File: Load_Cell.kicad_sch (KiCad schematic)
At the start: 1 part, among them J1 Conn_01x04

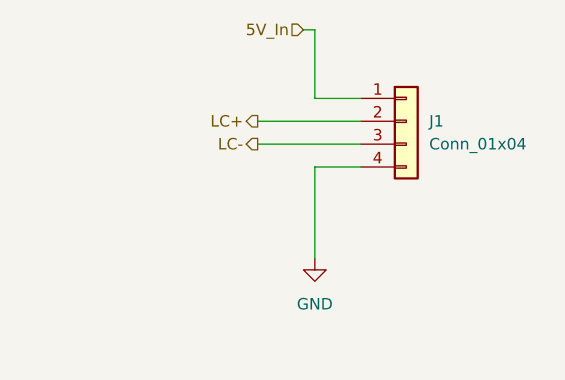
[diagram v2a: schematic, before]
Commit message: fix load cell connector
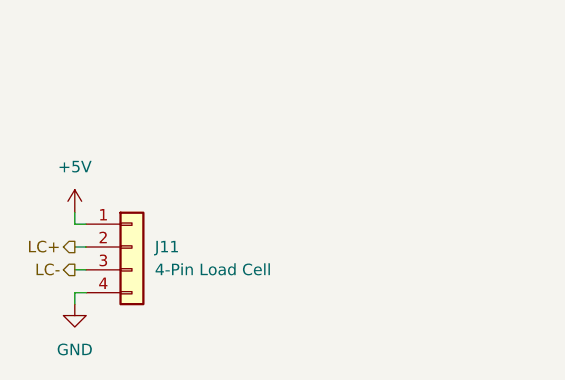
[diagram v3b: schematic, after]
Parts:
- removed J1: Conn_01x04, Connector_JST:JST_EH_B4B-EH-A_1x04_P2.50mm_Vertical, symbol Connector_Generic:Conn_01x04
- added J11: 4-Pin Load Cell, Connector_Molex:Molex_Micro-Fit_3.0_43650-0415_1x04_P3.00mm_Vertical, symbol Connector_Generic:Conn_01x04
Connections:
- net GND: now also J11.4 (Pin_4)
- net LC+: now also J11.2 (Pin_2)
- net LC-: now also J11.3 (Pin_3)
- new net +5V: J11.1 (Pin_1)
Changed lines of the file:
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@@
 	(wire
 		(pts
-			(xy 165.1 82.55) (xy 170.18 82.55)
-		)
-		(stroke
-			(width 0)
-			(type default)
-		)
-	)
-	(wire
-		(pts
-			(xy 163.83 74.93) (xy 165.1 74.93)
-		)
-		(stroke
-			(width 0)
-			(type default)
-		)
-	)
-	(wire
-		(pts
-			(xy 158.75 87.63) (xy 170.18 87.63)
-		)
-		(stroke
-			(width 0)
-			(type default)
-		)
-	)
-	(wire
-		(pts
-			(xy 165.1 100.33) (xy 165.1 90.17)
-		)
-		(stroke
-			(width 0)
-			(type default)
-		)
-	)
-	(wire
-		(pts
-			(xy 158.75 85.09) (xy 170.18 85.09)
-		)
-		(stroke
-			(width 0)
-			(type default)
-		)
-	)
-	(wire
-		(pts
-			(xy 165.1 90.17) (xy 170.18 90.17)
-		)
-		(stroke
-			(width 0)
-			(type default)
-		)
-	)
-	(wire
-		(pts
-			(xy 165.1 74.93) (xy 165.1 82.55)
+			(xy 138.43 101.6) (xy 139.7 101.6)
+		)
+		(stroke
+			(width 0)
+			(type default)
+		)
+	)
+	(wire
+		(pts
+			(xy 138.43 95.25) (xy 138.43 96.52)
+		)
+		(stroke
+			(width 0)
+			(type default)
+		)
+	)
+	(wire
+		(pts
+			(xy 138.43 105.41) (xy 138.43 104.14)
+		)
+		(stroke
+			(width 0)
+			(type default)
+		)
+	)
+	(wire
+		(pts
+			(xy 138.43 99.06) (xy 139.7 99.06)
+		)
+		(stroke
+			(width 0)
+			(type default)
+		)
+	)
+	(wire
+		(pts
+			(xy 138.43 96.52) (xy 139.7 96.52)
+		)
+		(stroke
+			(width 0)
+			(type default)
+		)
+	)
+	(wire
+		(pts
+			(xy 138.43 104.14) (xy 139.7 104.14)
 		)
 		(stroke
@@
 	(hierarchical_label "LC-"
 		(shape output)
-		(at 158.75 87.63 180)
+		(at 138.43 101.6 180)
 		(effects
 			(font
@@
 		)
 	)
-	(hierarchical_label "5V_In"
-		(shape input)
-		(at 163.83 74.93 180)
+	(hierarchical_label "LC+"
+		(shape output)
+		(at 138.43 99.06 180)
 		(effects
 			(font
@@
 		)
 	)
-	(hierarchical_label "LC+"
-		(shape output)
-		(at 158.75 85.09 180)
-		(effects
-			(font
-				(size 1.27 1.27)
-			)
-			(justify right)
-		)
-	)
 	(symbol
 		(lib_id "power:GND")
-		(at 165.1 100.33 0)
+		(at 138.43 105.41 0)
 		(unit 1)
 		(body_style 1)
@@
 		(fields_autoplaced yes)
 		(property "Reference" "#PWR0115"
-			(at 165.1 106.68 0)
+			(at 138.43 111.76 0)
 			(hide yes)
 			(show_name no)
@@
 		)
 		(property "Value" "GND"
-			(at 165.1 105.41 0)
+			(at 138.43 110.49 0)
 			(show_name no)
 			(do_not_autoplace no)
@@
 		)
 		(property "Footprint" ""
-			(at 165.1 100.33 0)
+			(at 138.43 105.41 0)
 			(hide yes)
 			(show_name no)
@@
 		)
 		(property "Datasheet" ""
-			(at 165.1 100.33 0)
+			(at 138.43 105.41 0)
 			(hide yes)
 			(show_name no)
@@
 		)
 		(property "Description" "Power symbol creates a global label with name \"GND\" , ground"
-			(at 165.1 100.33 0)
+			(at 138.43 105.41 0)
 			(hide yes)
 			(show_name no)
@@
 	)
 	(symbol
-		(lib_id "Connector_Generic:Conn_01x04")
-		(at 175.26 85.09 0)
+		(lib_id "power:+5V")
+		(at 138.43 95.25 0)
 		(unit 1)
 		(body_style 1)
@@
 		(dnp no)
 		(fields_autoplaced yes)
-		(property "Reference" "J1"
-			(at 177.8 85.0899 0)
-			(show_name no)
-			(do_not_autoplace no)
-			(effects
-				(font
-					(size 1.27 1.27)
-				)
-				(justify left)
-			)
-		)
-		(property "Value" "Conn_01x04"
-			(at 177.8 87.6299 0)
-			(show_name no)
-			(do_not_autoplace no)
-			(effects
-				(font
-					(size 1.27 1.27)
-				)
-				(justify left)
-			)
-		)
-		(property "Footprint" "Connector_JST:JST_EH_B4B-EH-A_1x04_P2.50mm_Vertical"
-			(at 175.26 85.09 0)
+		(property "Reference" "#PWR01"
+			(at 138.43 99.06 0)
+			(hide yes)
+			(show_name no)
+			(do_not_autoplace no)
+			(effects
+				(font
+					(size 1.27 1.27)
+				)
+			)
+		)
+		(property "Value" "+5V"
+			(at 138.43 90.17 0)
+			(show_name no)
+			(do_not_autoplace no)
+			(effects
+				(font
+					(size 1.27 1.27)
+				)
+			)
+		)
+		(property "Footprint" ""
+			(at 138.43 95.25 0)
 			(hide yes)
 			(show_name no)
@@
 		)
 		(property "Datasheet" ""
-			(at 175.26 85.09 0)
-			(hide yes)
-			(show_name no)
-			(do_not_autoplace no)
-			(effects
-				(font
-					(size 1.27 1.27)
-				)
-			)
-		)
-		(property "Description" "Generic connector, single row, 01x04, script generated (kicad-library-utils/schlib/autogen/connector/)"
-			(at 175.26 85.09 0)
-			(hide yes)
-			(show_name no)
-			(do_not_autoplace no)
-			(effects
-				(font
-					(size 1.27 1.27)
-				)
-			)
-		)
-		(pin "2"
-		)
-		(pin "4"
+			(at 138.43 95.25 0)
+			(hide yes)
+			(show_name no)
+			(do_not_autoplace no)
+			(effects
+				(font
+					(size 1.27 1.27)
+				)
+			)
+		)
+		(property "Description" "Power symbol creates a global label with name \"+5V\""
+			(at 138.43 95.25 0)
+			(hide yes)
+			(show_name no)
+			(do_not_autoplace no)
+			(effects
+				(font
+					(size 1.27 1.27)
+				)
+			)
 		)
 		(pin "1"
-		)
-		(pin "3"
 		)
 		(instances
 			(project "gse_control_node"
 				(path "/24817451-dfe0-4b9a-9d93-7304529c9d58/3fe78498-f3da-4a4e-905d-c6815bbc6a4f"
-					(reference "J1")
+					(reference "#PWR01")
 					(unit 1)
 				)
+			)
+		)
+	)
+	(symbol
+		(lib_id "Connector_Generic:Conn_01x04")
+		(at 144.78 99.06 0)
+		(unit 1)
+		(body_style 1)
+		(exclude_from_sim no)
+		(in_bom no)
+		(on_board yes)
+		(in_pos_files yes)
+		(dnp no)
+		(fields_autoplaced yes)
+		(property "Reference" "J11"
+			(at 147.32 99.0599 0)
+			(show_name no)
+			(do_not_autoplace no)
+			(effects
+				(font
+					(size 1.27 1.27)
+				)
+				(justify left)
+			)
+		)
+		(property "Value" "4-Pin Load Cell"
+			(at 147.32 101.5999 0)
+			(show_name no)
+			(do_not_autoplace no)
+			(effects
+				(font
+					(size 1.27 1.27)
+				)
+				(justify left)
+			)
+		)
+		(property "Footprint" "Connector_Molex:Molex_Micro-Fit_3.0_43650-0415_1x04_P3.00mm_Vertical"
+			(at 144.78 99.06 0)
+			(hide yes)
+			(show_name no)
+			(do_not_autoplace no)
+			(effects
+				(font
+					(size 1.27 1.27)
+				)
+			)
+		)
+		(property "Datasheet" ""
+			(at 144.78 99.06 0)
+			(hide yes)
+			(show_name no)
+			(do_not_autoplace no)
+			(effects
+				(font
+					(size 1.27 1.27)
+				)
+			)
+		)
+		(property "Description" "Generic connector, single row, 01x04, script generated (kicad-library-utils/schlib/autogen/connector/)"
+			(at 144.78 99.06 0)
+			(hide yes)
+			(show_name no)
+			(do_not_autoplace no)
+			(effects
+				(font
+					(size 1.27 1.27)
+				)
+			)
+		)
+		(property "ADC Number" ""
+			(at 144.78 99.06 0)
+			(hide yes)
+			(show_name no)
+			(do_not_autoplace no)
+			(effects
+				(font
+					(size 1.27 1.27)
+				)
+			)
+		)
+		(property "DCR" ""
+			(at 144.78 99.06 0)
+			(hide yes)
+			(show_name no)
+			(do_not_autoplace no)
+			(effects
+				(font
+					(size 1.27 1.27)
+				)
+			)
+		)
+		(property "I2C Address" ""
+			(at 144.78 99.06 0)
+			(hide yes)
+			(show_name no)
+			(do_not_autoplace no)
+			(effects
+				(font
+					(size 1.27 1.27)
+				)
+			)
+		)
+		(property "Irated" ""
+			(at 144.78 99.06 0)
+			(hide yes)
+			(show_name no)
+			(do_not_autoplace no)
+			(effects
+				(font
+					(size 1.27 1.27)
+				)
+			)
+		)
+		(property "Isat" ""
+			(at 144.78 99.06 0)
+			(hide yes)
+			(show_name no)
+			(do_not_autoplace no)
+			(effects
+				(font
+					(size 1.27 1.27)
+				)
+			)
+		)
+		(property "MFG" ""
+			(at 144.78 99.06 0)
+			(hide yes)
+			(show_name no)
+			(do_not_autoplace no)
+			(effects
+				(font
+					(size 1.27 1.27)
+				)
+			)
+		)
+		(property "MFR" ""
+			(at 144.78 99.06 0)
+			(hide yes)
+			(show_name no)
+			(do_not_autoplace no)
+			(effects
+				(font
+					(size 1.27 1.27)
+				)
+			)
+		)
+		(pin "4"
+		)
+		(pin "2"
+		)
+		(pin "1"
+		)
+		(pin "3"
+		)
+		(instances
+			(project "gse_control_node"
+				(path "/24817451-dfe0-4b9a-9d93-7304529c9d58/3fe78498-f3da-4a4e-905d-c6815bbc6a4f"
+					(reference "J11")
+					(unit 1)
+				)
